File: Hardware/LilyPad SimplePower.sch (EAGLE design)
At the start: 10 parts

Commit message: Hardware Version 2.0 commit
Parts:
- removed JP2: (no value), SparkFun-Passives:JUMPER-2SMD-NC
- added C1, C2: 4.7uF, SparkFun-Capacitors:4.7UF-6.3V-10%(0603)0603
- added D1: (no value), SparkFun-LED:LED-YELLOW0603
- added H1, H2: SEW_HOLE, LilyPad-Wearables:SEW_HOLE
- added JP4: USB_MICROB_PLUGCONN-11752, SparkFun-Connectors:USB_MICROB_PLUGCONN-11752
- added R3: 330, SparkFun-Resistors:330OHM1/10W1%(0603)
- added R4: 2.0k, SparkFun-Resistors:2.0KOHM1/10W5%(0603)
- added SJ1: SOLDERJUMPERTRACE, SparkFun-Passives:SOLDERJUMPERTRACE
- added U1: MCP73831, SparkFun-PowerIC:MCP73831
- U$3, U$4: value SEWTAP7 -> SEWTAP9; device LilyPad-Wearables:SEWTAP7 -> LilyPad-Wearables:SEWTAP9
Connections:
- new net N$3: C1.1, JP4.VCC, R3.1, U1.VIN
- new net N$4: D1.C, U1.STAT
- new net N$5: D1.A, R3.2
- new net N$7: R4.2, U1.PROG
- net +: now also SJ1.2; no longer JP2.2
- net GND: now also C1.2, C2.2, JP4.GND, R4.1, U1.VSS
- net N$1: now also C2.1, U1.VBAT
- net N$2: now also SJ1.1; no longer JP2.1
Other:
- moved on the sheet: JP1, R1, R2, S1

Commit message: Adding review changes
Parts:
- added U$6: REVISION, SparkFun-Aesthetics:REVISION
- SJ1: value SOLDERJUMPERTRACE -> SOLDERJUMPERNC; device SparkFun-Passives:SOLDERJUMPERTRACE -> SparkFun-Passives:SOLDERJUMPERNC
- U$1: value LOGO-LPL -> LOGO-LPLP; device LilyPad-Wearables:LOGO-LPL -> LilyPad-Wearables:LOGO-LPLP
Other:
- note added: "Charging Rate = 500 mA"
- note added: "Nathan Seidle"
- note added: "Sew Taps- Not Connected"
- note added: "Toni Klopfenstein"
- note added: "User provided resistor: Either PTH or SMD"
- note added: "v 2.0"
- note removed: "Either PTH or SMD"
- note removed: "N.Seidle, T.Klopfenstein"
- note removed: "User provided resistor"
- moved on the sheet: C1, C2, D1, H1, H2, JP1, JP4, R1, R2, R3, R4, S1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

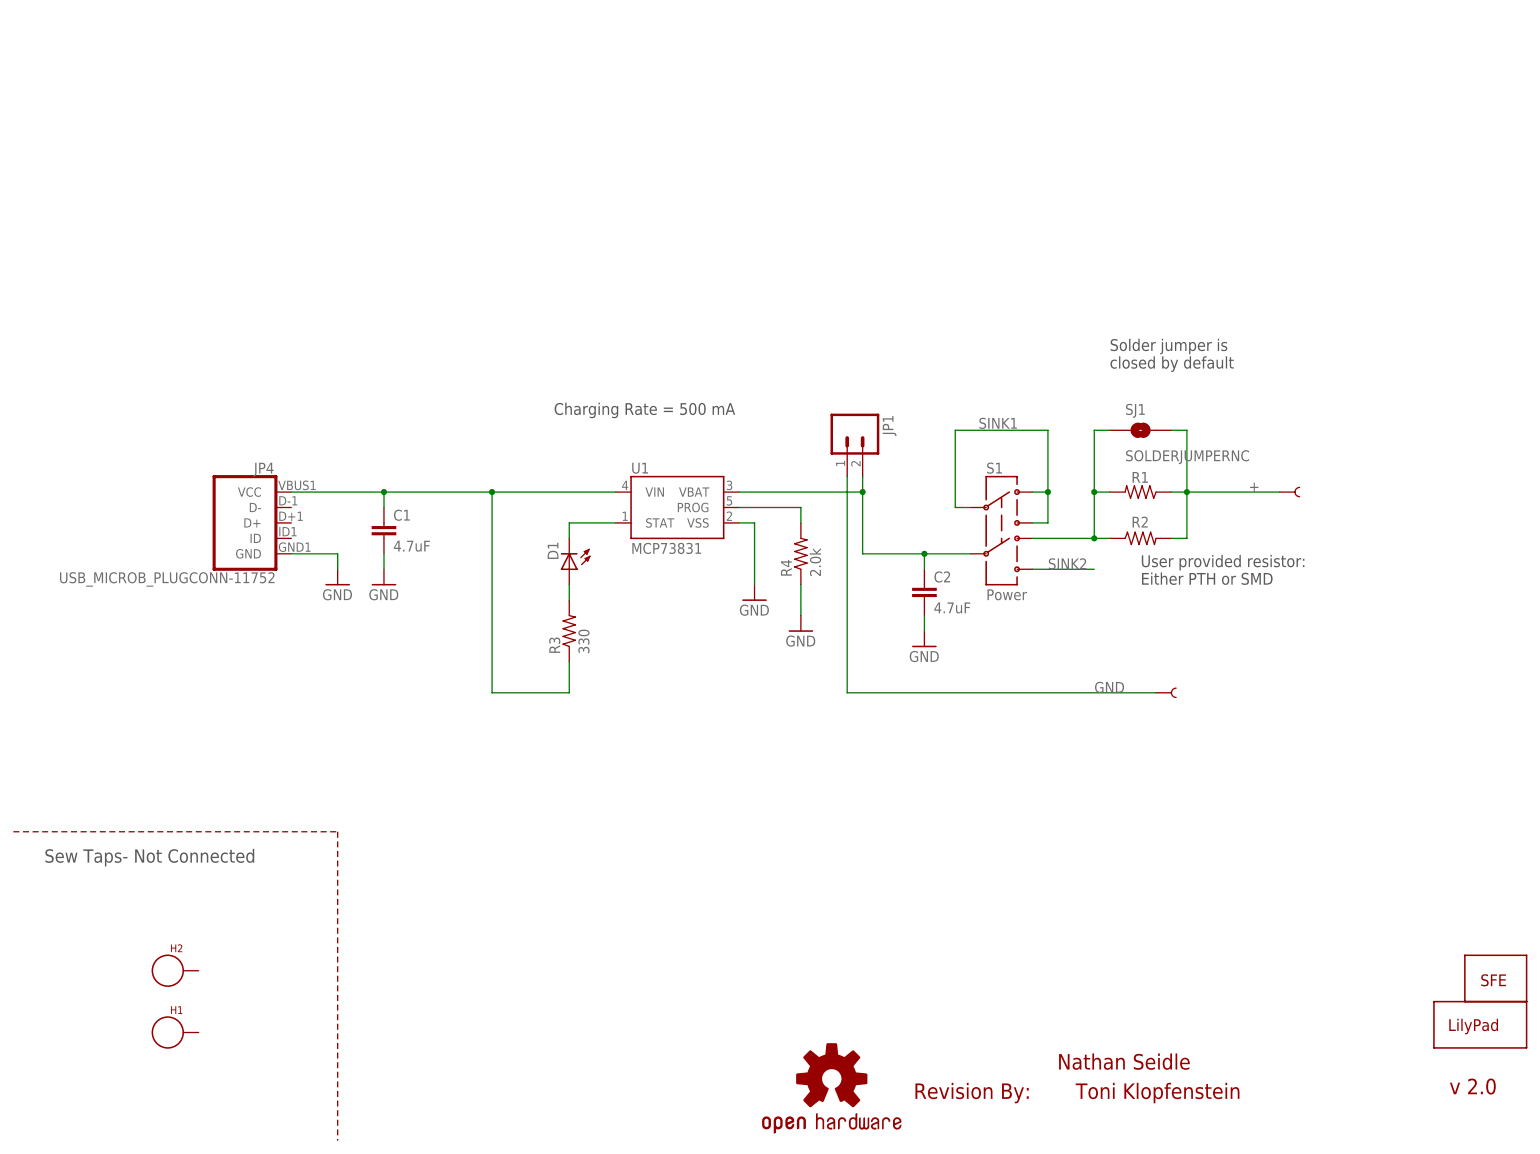
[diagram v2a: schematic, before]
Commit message: Fixing PWR label to CHG on LED
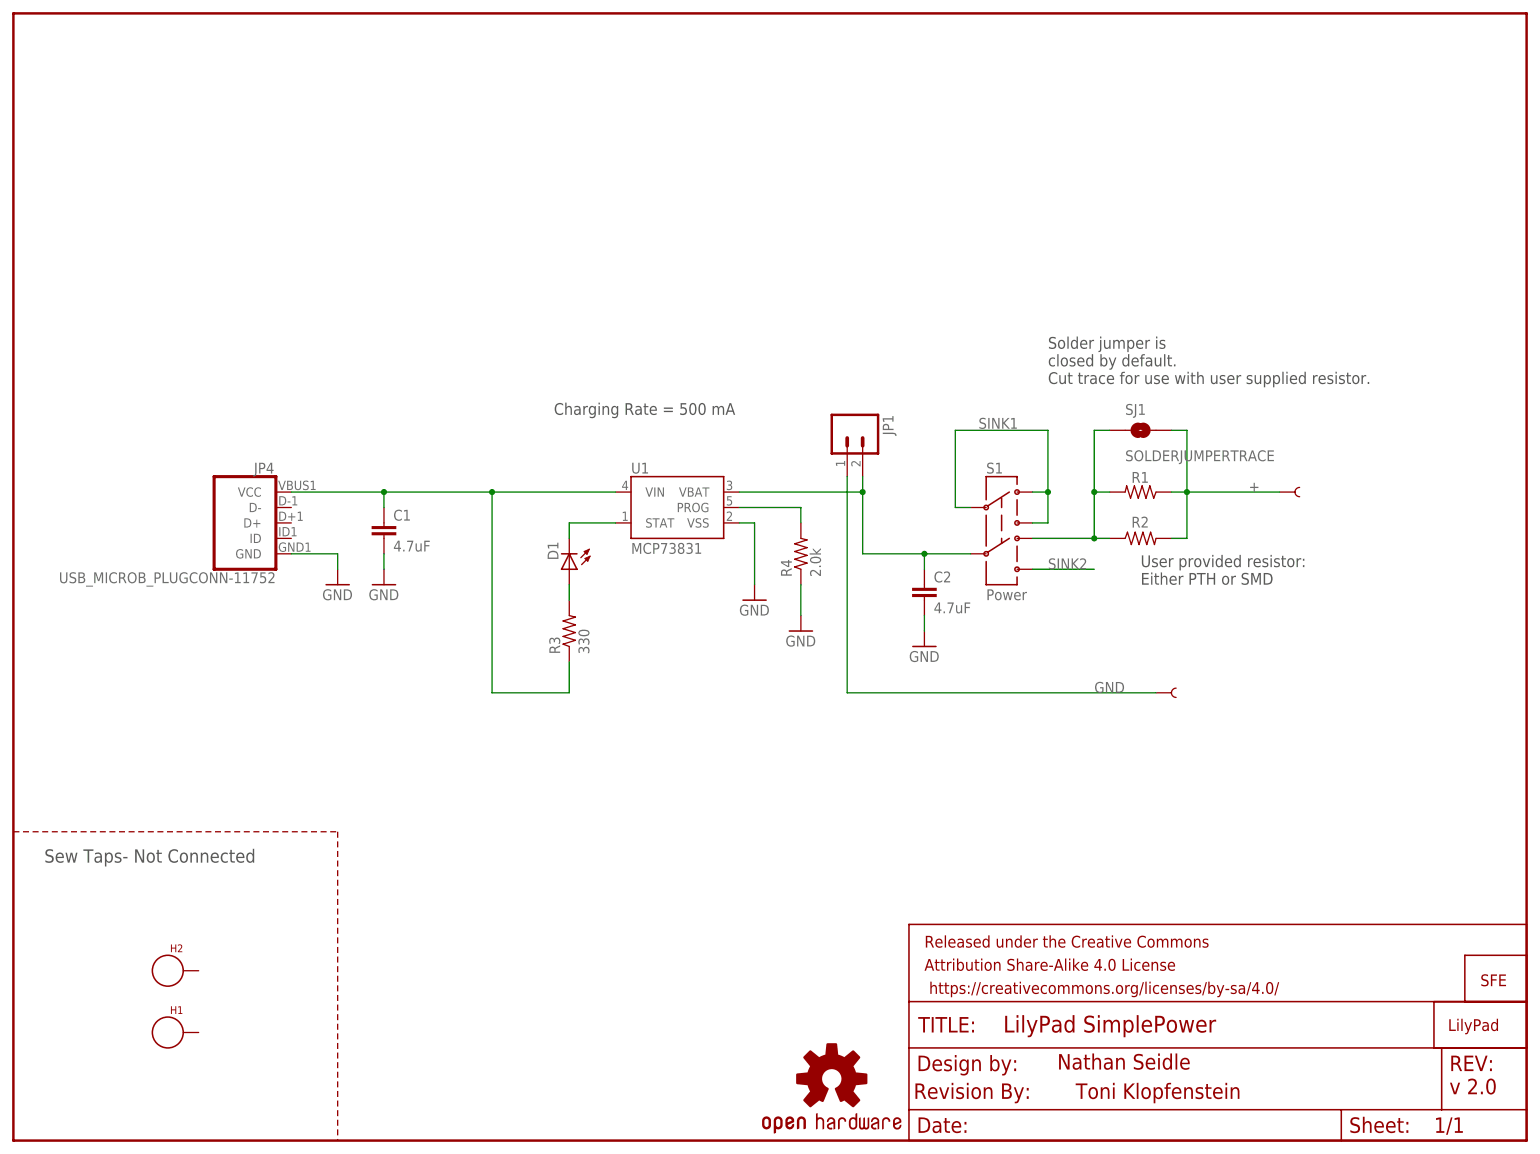
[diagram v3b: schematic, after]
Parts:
- added FRAME1: FRAME-LETTER, SparkFun-Aesthetics:FRAME-LETTER
- SJ1: value SOLDERJUMPERNC -> SOLDERJUMPERTRACE; device SparkFun-Passives:SOLDERJUMPERNC -> SparkFun-Passives:SOLDERJUMPERTRACE
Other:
- note added: "Solder jumper is closed by default. Cut trace for use with user supplied resistor."
- note removed: "Solder jumper is closed by default"
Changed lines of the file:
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@@
 <grid distance="0.1" unitdist="inch" unit="inch" style="lines" multiple="1" display="no" altdistance="0.01" altunitdist="inch" altunit="inch"/>
 <layers>
-<layer number="1" name="Top" color="4" fill="1" visible="no" active="no"/>
-<layer number="2" name="Route2" color="1" fill="3" visible="no" active="no"/>
-<layer number="3" name="Route3" color="4" fill="3" visible="no" active="no"/>
-<layer number="4" name="Route4" color="1" fill="4" visible="no" active="no"/>
-<layer number="5" name="Route5" color="4" fill="4" visible="no" active="no"/>
-<layer number="6" name="Route6" color="1" fill="8" visible="no" active="no"/>
-<layer number="7" name="Route7" color="4" fill="8" visible="no" active="no"/>
-<layer number="8" name="Route8" color="1" fill="2" visible="no" active="no"/>
-<layer number="9" name="Route9" color="4" fill="2" visible="no" active="no"/>
-<layer number="10" name="Route10" color="1" fill="7" visible="no" active="no"/>
-<layer number="11" name="Route11" color="4" fill="7" visible="no" active="no"/>
-<layer number="12" name="Route12" color="1" fill="5" visible="no" active="no"/>
-<layer number="13" name="Route13" color="4" fill="5" visible="no" active="no"/>
-<layer number="14" name="Route14" color="1" fill="6" visible="no" active="no"/>
-<layer number="15" name="Route15" color="4" fill="6" visible="no" active="no"/>
-<layer number="16" name="Bottom" color="1" fill="1" visible="no" active="no"/>
-<layer number="17" name="Pads" color="2" fill="1" visible="no" active="no"/>
-<layer number="18" name="Vias" color="2" fill="1" visible="no" active="no"/>
-<layer number="19" name="Unrouted" color="6" fill="1" visible="no" active="no"/>
-<layer number="20" name="Dimension" color="15" fill="1" visible="no" active="no"/>
-<layer number="21" name="tPlace" color="16" fill="1" visible="no" active="no"/>
-<layer number="22" name="bPlace" color="14" fill="1" visible="no" active="no"/>
-<layer number="23" name="tOrigins" color="15" fill="1" visible="no" active="no"/>
-<layer number="24" name="bOrigins" color="15" fill="1" visible="no" active="no"/>
-<layer number="25" name="tNames" color="7" fill="1" visible="no" active="no"/>
-<layer number="26" name="bNames" color="7" fill="1" visible="no" active="no"/>
-<layer number="27" name="tValues" color="7" fill="1" visible="no" active="no"/>
-<layer number="28" name="bValues" color="7" fill="1" visible="no" active="no"/>
+<layer number="1" name="Top" color="4" fill="1" visible="yes" active="no"/>
+<layer number="2" name="Route2" color="1" fill="3" visible="yes" active="no"/>
+<layer number="3" name="Route3" color="4" fill="3" visible="yes" active="no"/>
+<layer number="4" name="Route4" color="1" fill="4" visible="yes" active="no"/>
+<layer number="5" name="Route5" color="4" fill="4" visible="yes" active="no"/>
+<layer number="6" name="Route6" color="1" fill="8" visible="yes" active="no"/>
+<layer number="7" name="Route7" color="4" fill="8" visible="yes" active="no"/>
+<layer number="8" name="Route8" color="1" fill="2" visible="yes" active="no"/>
+<layer number="9" name="Route9" color="4" fill="2" visible="yes" active="no"/>
+<layer number="10" name="Route10" color="1" fill="7" visible="yes" active="no"/>
+<layer number="11" name="Route11" color="4" fill="7" visible="yes" active="no"/>
+<layer number="12" name="Route12" color="1" fill="5" visible="yes" active="no"/>
+<layer number="13" name="Route13" color="4" fill="5" visible="yes" active="no"/>
+<layer number="14" name="Route14" color="1" fill="6" visible="yes" active="no"/>
+<layer number="15" name="Route15" color="4" fill="6" visible="yes" active="no"/>
+<layer number="16" name="Bottom" color="1" fill="1" visible="yes" active="no"/>
+<layer number="17" name="Pads" color="2" fill="1" visible="yes" active="no"/>
+<layer number="18" name="Vias" color="2" fill="1" visible="yes" active="no"/>
+<layer number="19" name="Unrouted" color="6" fill="1" visible="yes" active="no"/>
+<layer number="20" name="Dimension" color="15" fill="1" visible="yes" active="no"/>
+<layer number="21" name="tPlace" color="16" fill="1" visible="yes" active="no"/>
+<layer number="22" name="bPlace" color="14" fill="1" visible="yes" active="no"/>
+<layer number="23" name="tOrigins" color="15" fill="1" visible="yes" active="no"/>
+<layer number="24" name="bOrigins" color="15" fill="1" visible="yes" active="no"/>
+<layer number="25" name="tNames" color="7" fill="1" visible="yes" active="no"/>
+<layer number="26" name="bNames" color="7" fill="1" visible="yes" active="no"/>
+<layer number="27" name="tValues" color="7" fill="1" visible="yes" active="no"/>
+<layer number="28" name="bValues" color="7" fill="1" visible="yes" active="no"/>
 <layer number="29" name="tStop" color="13" fill="3" visible="no" active="no"/>
 <layer number="30" name="bStop" color="7" fill="6" visible="no" active="no"/>
@@
 <layer number="35" name="tGlue" color="7" fill="4" visible="no" active="no"/>
 <layer number="36" name="bGlue" color="7" fill="5" visible="no" active="no"/>
-<layer number="37" name="tTest" color="7" fill="1" visible="no" active="no"/>
-<layer number="38" name="bTest" color="7" fill="1" visible="no" active="no"/>
+<layer number="37" name="tTest" color="7" fill="1" visible="yes" active="no"/>
+<layer number="38" name="bTest" color="7" fill="1" visible="yes" active="no"/>
 <layer number="39" name="tKeepout" color="4" fill="11" visible="no" active="no"/>
 <layer number="40" name="bKeepout" color="1" fill="11" visible="no" active="no"/>
@@
 <layer number="44" name="Drills" color="7" fill="1" visible="no" active="no"/>
 <layer number="45" name="Holes" color="7" fill="1" visible="no" active="no"/>
-<layer number="46" name="Milling" color="3" fill="1" visible="no" active="no"/>
-<layer number="47" name="Measures" color="7" fill="1" visible="no" active="no"/>
-<layer number="48" name="Document" color="7" fill="1" visible="no" active="no"/>
-<layer number="49" name="Reference" color="7" fill="1" visible="no" active="no"/>
-<layer number="50" name="dxf" color="7" fill="1" visible="no" active="no"/>
-<layer number="51" name="tDocu" color="6" fill="1" visible="no" active="no"/>
-<layer number="52" name="bDocu" color="7" fill="1" visible="no" active="no"/>
-<layer number="53" name="tGND_GNDA" color="7" fill="9" visible="no" active="no"/>
-<layer number="54" name="bGND_GNDA" color="1" fill="9" visible="no" active="no"/>
-<layer number="56" name="wert" color="7" fill="1" visible="no" active="no"/>
+<layer number="46" name="Milling" color="3" fill="1" visible="yes" active="no"/>
+<layer number="47" name="Measures" color="7" fill="1" visible="yes" active="no"/>
+<layer number="48" name="Document" color="7" fill="1" visible="yes" active="no"/>
+<layer number="49" name="Reference" color="7" fill="1" visible="yes" active="no"/>
+<layer number="50" name="dxf" color="7" fill="1" visible="yes" active="no"/>
+<layer number="51" name="tDocu" color="6" fill="1" visible="yes" active="no"/>
+<layer number="52" name="bDocu" color="7" fill="1" visible="yes" active="no"/>
+<layer number="53" name="tGND_GNDA" color="7" fill="9" visible="yes" active="no"/>
+<layer number="54" name="bGND_GNDA" color="1" fill="9" visible="yes" active="no"/>
+<layer number="56" name="wert" color="7" fill="1" visible="yes" active="no"/>
 <layer number="91" name="Nets" color="2" fill="1" visible="yes" active="yes"/>
 <layer number="92" name="Busses" color="1" fill="1" visible="yes" active="yes"/>
@@
 <part name="R4" library="SparkFun-Resistors" deviceset="2.0KOHM1/10W5%(0603)" device="" value="2.0k"/>
 <part name="GND5" library="SparkFun-Aesthetics" deviceset="GND" device=""/>
-<part name="SJ1" library="SparkFun-Passives" deviceset="SOLDERJUMPER" device="NC" value="SOLDERJUMPERNC"/>
+<part name="SJ1" library="SparkFun-Passives" deviceset="SOLDERJUMPER" device="TRACE" value="SOLDERJUMPERTRACE"/>
 <part name="H1" library="LilyPad-Wearables" deviceset="SEW_HOLE" device=""/>
 <part name="H2" library="LilyPad-Wearables" deviceset="SEW_HOLE" device=""/>
@@
 <text x="185.42" y="91.44" size="1.9304" layer="97">User provided resistor:
 Either PTH or SMD</text>
-<text x="180.34" y="127" size="1.9304" layer="97" font="vector">Solder jumper is
-closed by default</text>
+<text x="170.18" y="124.46" size="1.9304" layer="97" font="vector">Solder jumper is
+closed by default.
+Cut trace for use with user supplied resistor.</text>
 <text x="171.704" y="11.684" size="2.54" layer="94">Nathan Seidle</text>
 <text x="236.22" y="7.62" size="2.54" layer="94">v 2.0</text>

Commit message: midway work  on updating design
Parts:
- removed R1: (no value), SparkFun:RESISTORAXIAL-0.3
- removed R2: (no value), SparkFun:RESISTOR1206
- removed SJ1: SOLDERJUMPERTRACE, SparkFun-Passives:SOLDERJUMPERTRACE
- added H3, H4: SEW_HOLE, LilyPad-Wearables:SEW_HOLE
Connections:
- removed net +: R1.1, R2.2, SJ1.2, U$4.1
- removed net N$2: R1.2, R2.1, S1.4, SJ1.1
- removed net SINK2: S1.6
- new net N$6: S1.4, U$4.1
- net GND: now also S1.6
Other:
- note removed: "Solder jumper is closed by default. Cut trace for use with user supplied resistor."
- note removed: "User provided resistor: Either PTH or SMD"
- moved on the sheet: C1, C2, D1, H1, H2, JP1, JP4, R3, R4, S1, U1

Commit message: More petal work
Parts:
- H1: value SEW_HOLE -> SEWTAP4; device LilyPad-Wearables:SEW_HOLE -> LilyPad-Wearables:SEWTAP4
- H2, H3, H4: value SEW_HOLE -> SEWTAP6; device LilyPad-Wearables:SEW_HOLE -> LilyPad-Wearables:SEWTAP6
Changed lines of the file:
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@@
 <part name="GND5" library="SparkFun-Aesthetics" deviceset="GND" device=""/>
 <part name="U$6" library="SparkFun-Aesthetics" deviceset="REVISION" device=""/>
-<part name="H1" library="LilyPad-Wearables" deviceset="SEW_HOLE" device=""/>
-<part name="H2" library="LilyPad-Wearables" deviceset="SEW_HOLE" device=""/>
-<part name="H3" library="LilyPad-Wearables" deviceset="SEW_HOLE" device=""/>
-<part name="H4" library="LilyPad-Wearables" deviceset="SEW_HOLE" device=""/>
+<part name="H1" library="LilyPad-Wearables" deviceset="SEWTAP" device="4"/>
+<part name="H2" library="LilyPad-Wearables" deviceset="SEWTAP" device="6"/>
+<part name="H3" library="LilyPad-Wearables" deviceset="SEWTAP" device="6"/>
+<part name="H4" library="LilyPad-Wearables" deviceset="SEWTAP" device="6"/>
 </parts>
 <sheets>

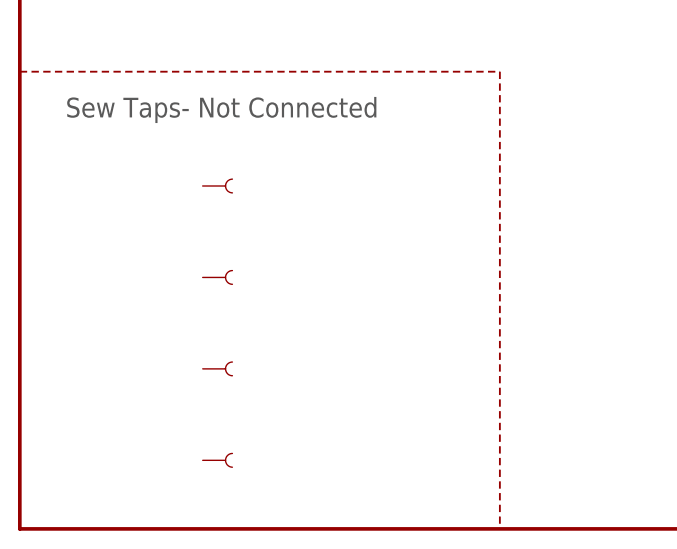
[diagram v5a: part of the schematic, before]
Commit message: Initial polygon pours corrected
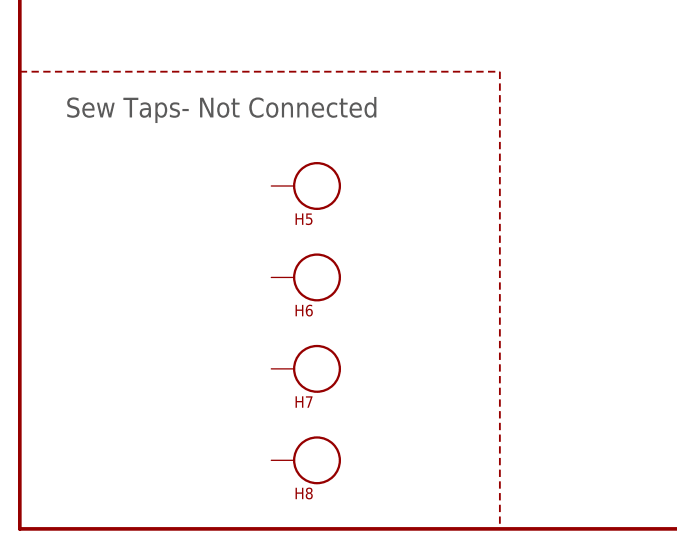
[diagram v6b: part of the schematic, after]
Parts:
- removed H1: SEWTAP4, LilyPad-Wearables:SEWTAP4
- removed H2, H3, H4: SEWTAP6, LilyPad-Wearables:SEWTAP6
- added H5, H6, H7, H8: SEW_HOLE, LilyPad-Wearables:SEW_HOLE
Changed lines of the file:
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@@
 <part name="GND5" library="SparkFun-Aesthetics" deviceset="GND" device=""/>
 <part name="U$6" library="SparkFun-Aesthetics" deviceset="REVISION" device=""/>
-<part name="H1" library="LilyPad-Wearables" deviceset="SEWTAP" device="4"/>
-<part name="H2" library="LilyPad-Wearables" deviceset="SEWTAP" device="6"/>
-<part name="H3" library="LilyPad-Wearables" deviceset="SEWTAP" device="6"/>
-<part name="H4" library="LilyPad-Wearables" deviceset="SEWTAP" device="6"/>
+<part name="H5" library="LilyPad-Wearables" deviceset="SEW_HOLE" device=""/>
+<part name="H6" library="LilyPad-Wearables" deviceset="SEW_HOLE" device=""/>
+<part name="H7" library="LilyPad-Wearables" deviceset="SEW_HOLE" device=""/>
+<part name="H8" library="LilyPad-Wearables" deviceset="SEW_HOLE" device=""/>
 </parts>
 <sheets>
@@
 <instance part="GND5" gate="1" x="157.48" y="96.52"/>
 <instance part="U$6" gate="G$1" x="148.082" y="6.858"/>
-<instance part="H1" gate="G$1" x="22.86" y="38.1"/>
-<instance part="H2" gate="G$1" x="22.86" y="27.94"/>
-<instance part="H3" gate="G$1" x="22.86" y="17.78"/>
-<instance part="H4" gate="G$1" x="22.86" y="7.62"/>
+<instance part="H5" gate="G$1" x="33.02" y="38.1"/>
+<instance part="H6" gate="G$1" x="33.02" y="27.94"/>
+<instance part="H7" gate="G$1" x="33.02" y="17.78"/>
+<instance part="H8" gate="G$1" x="33.02" y="7.62"/>
 </instances>
 <busses>
